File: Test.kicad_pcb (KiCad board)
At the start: 4 copper layers, 171.1 x 129.2 mm, 479 parts, among them P1 CONN_01X02, P18 CONN_01X02, P19 CONN_01X02, P2 CONN_01X02, P24 CONN_01X02, P3 CONN_01X05, P4 CONN_01X04, P8 CONN_01X02, Q1 BSC440N10NS3GATMA1, Q2 BSC440N10NS3GATMA1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

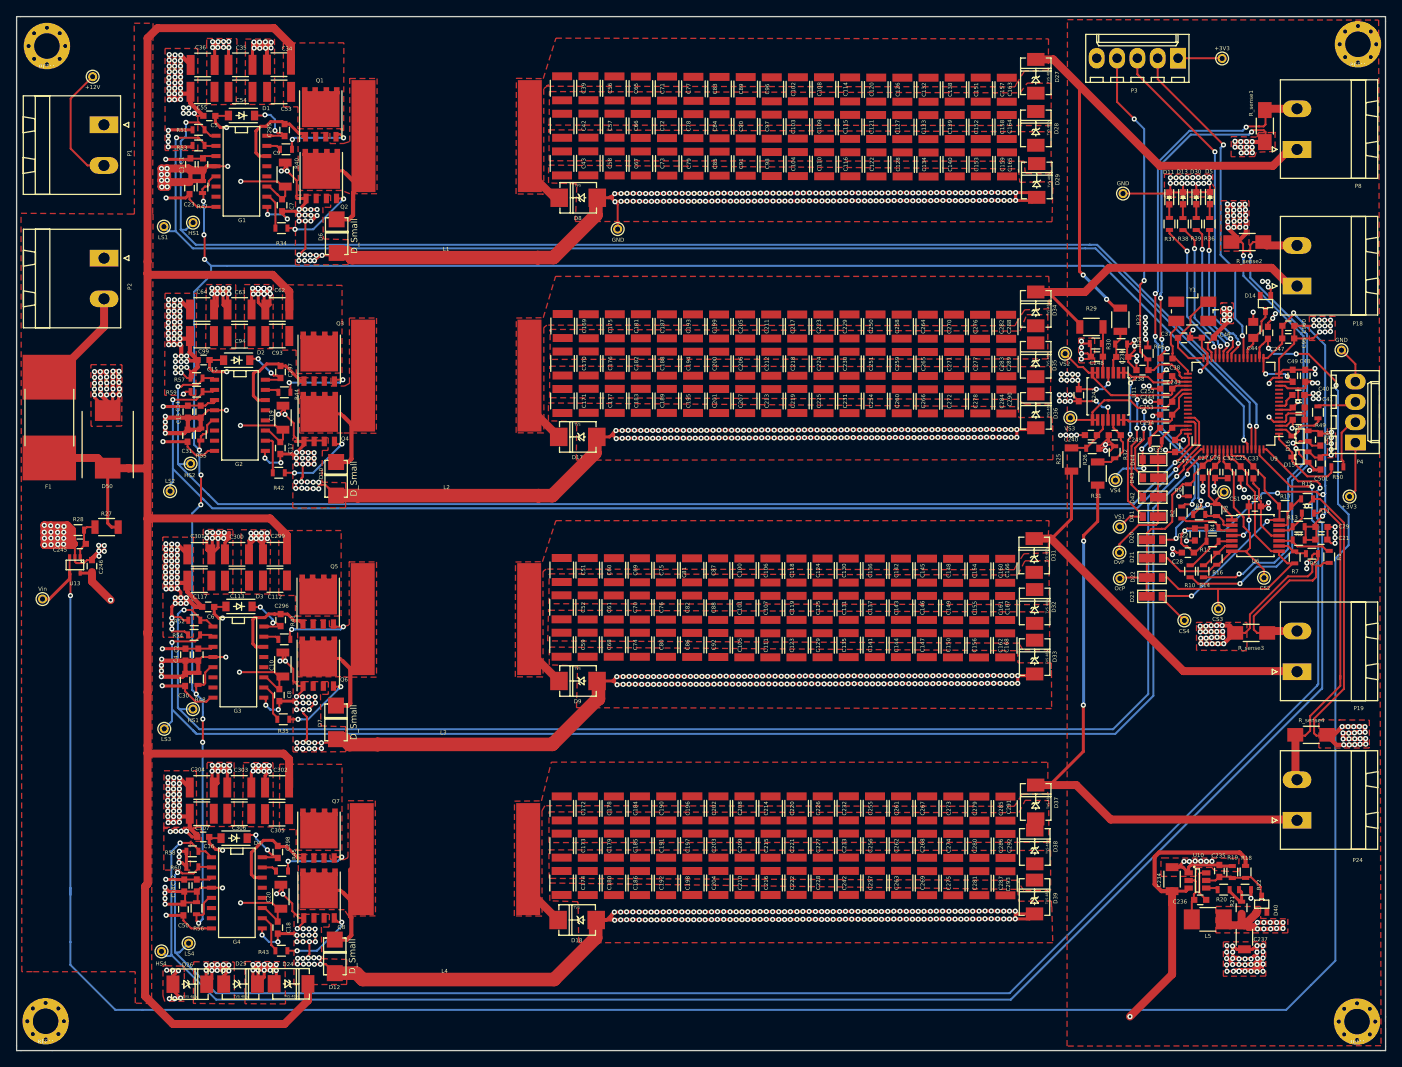
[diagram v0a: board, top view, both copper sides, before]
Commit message: Changed some Diodes footprints to achieve the recommended ones on the datasheet
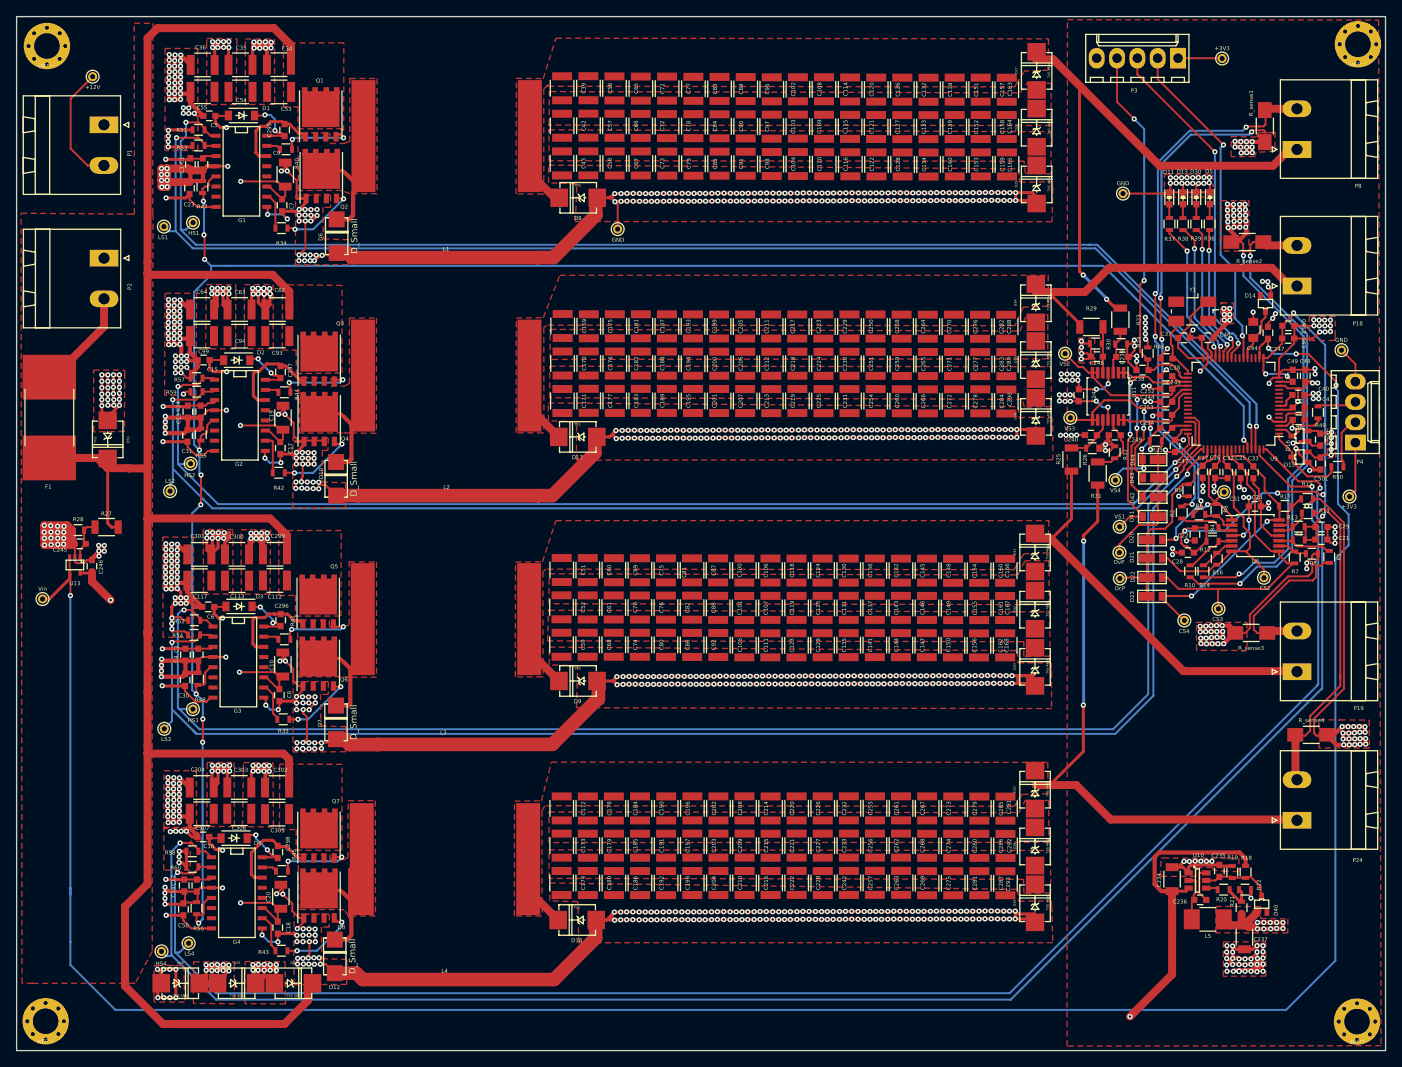
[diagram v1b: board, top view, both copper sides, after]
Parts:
- D24, D25, D26, D27, D28, D29, D31, D32, D33, D34, D35, D36, D37, D38, D39: footprint Eigene Footprints:DO-214AA_TVS_48V -> Eigene Footprints:DO-214AA_TVS_inp
- D50: footprint Diodes_SMD:DO-214AB -> Eigene Footprints:DO-214AA_TVS_inp
- moved D37 1.54 mm to (259.8, 190.2)
- moved D33 1.22 mm to (259.8, 174.8)
- moved D26 1.20 mm to (152.9, 214.3)
- moved D39 0.78 mm to (259.8, 204.3)
- moved D36 0.75 mm to (259.8, 143.6)
- moved D34 0.70 mm to (259.9, 129.3)
- moved D27 0.69 mm to (259.9, 100.3)
- moved D29 0.50 mm to (259.9, 114.5)
- moved D25 0.50 mm to (159.9, 214.3)
- moved D32 0.40 mm to (259.8, 167.7)
- moved D31 0.39 mm to (259.8, 160.5)
- moved D24 0.31 mm to (167.1, 214.3)
- moved D28 0.13 mm to (259.9, 107.4)
- moved D38 0.07 mm to (259.8, 197.2)
- turned D50 to 270 degrees
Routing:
- net GND: track 1547.0 -> 1551.5 mm, vias 1066 -> 1065
- net V_in-: track 253.4 -> 256.2 mm

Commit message: vias under Mosfets more cupper for GND general changes
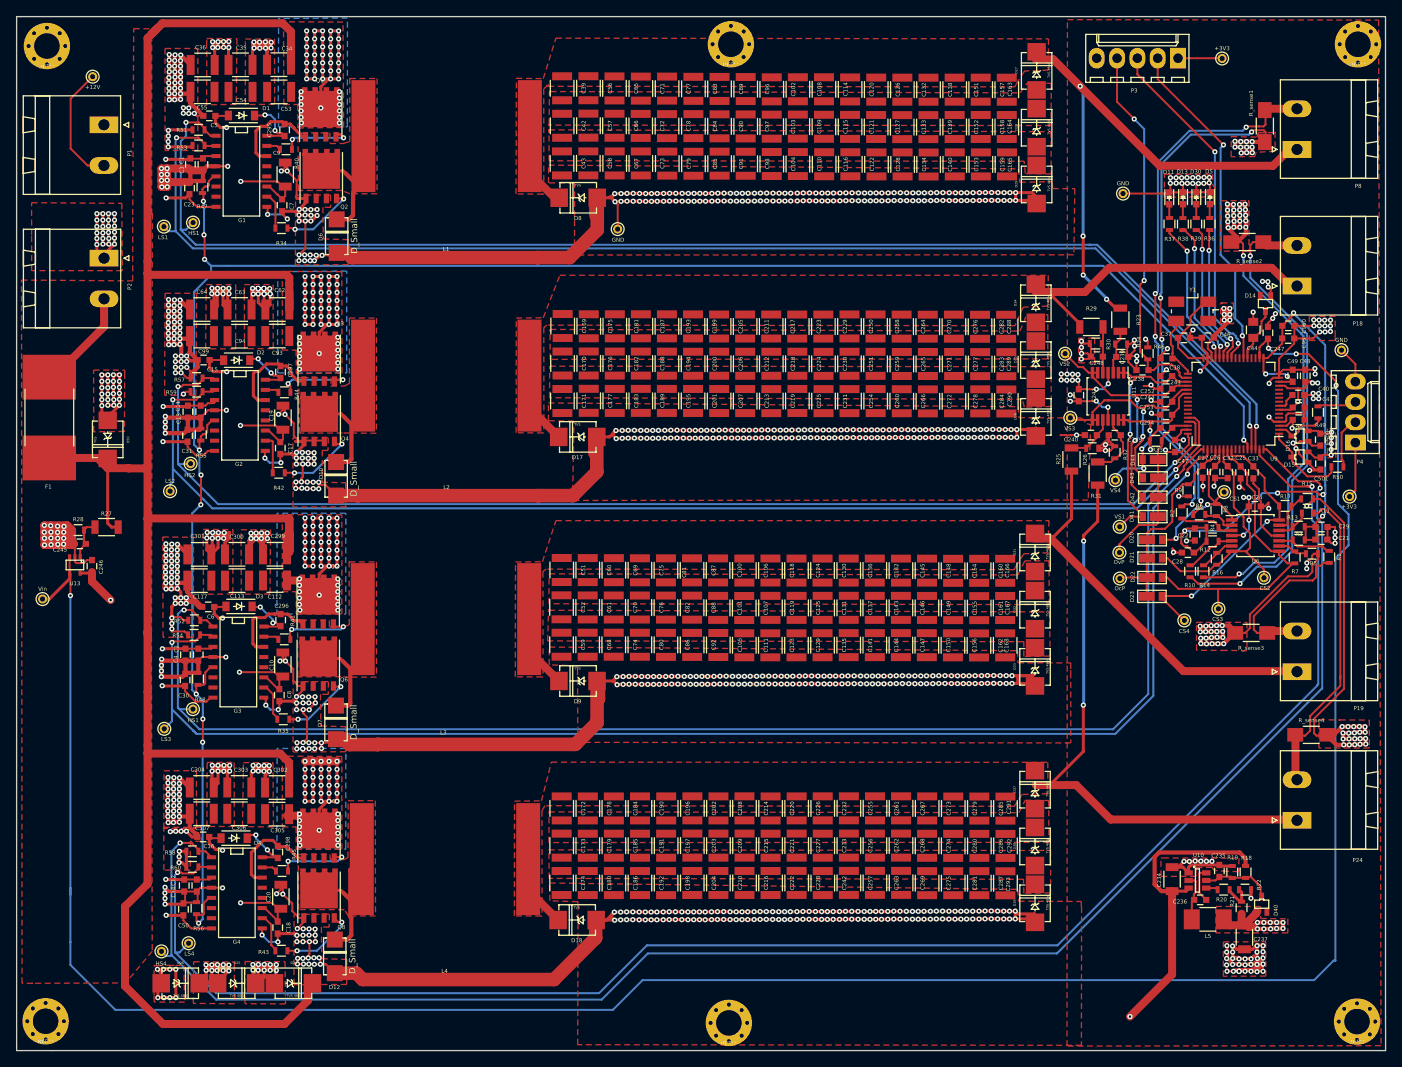
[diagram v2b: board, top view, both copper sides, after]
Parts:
- added REF**: 3mm_holes, Eigene Footprints:3mm_holes, F.Cu at (221.5, 219.3)
- added REF**: 3mm_holes, Eigene Footprints:3mm_holes, F.Cu at (221.7, 97.0)
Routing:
- net V_in-: track 256.2 -> 519.2 mm, vias 0 -> 187
- net GND: track 1551.5 -> 1569.6 mm, vias 1065 -> 1069
- net V_12V: track 388.2 -> 393.1 mm
- net V_out_1: track 84.2 -> 79.4 mm, vias 2 -> 4
- net Sense_Out_Volt_4: track 22.6 -> 24.1 mm
- net +3V3: track 472.9 -> 471.6 mm, vias 57 -> 53
- added copper zone on B.Cu, net V_in-

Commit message: O
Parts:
- G1, G2, G3, G4: footprint SMD_Packages:SO-16-N -> Eigene Footprints:SOIC-16_3.9x9.9mm_Pitch1.27mm
- moved +12V 4.83 mm to (142.2, 96.2)
- moved D4 0.16 mm to (159.7, 196.1)
- moved D2 0.11 mm to (160.0, 136.4)
- moved G1 0.10 mm to (160.4, 112.8), turned to 0 degrees
- moved G3 0.07 mm to (160.2, 174.2), turned to 0 degrees
- moved G2 0.06 mm to (160.4, 143.3), turned to 0 degrees
- turned G4 to 0 degrees
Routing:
- net GND: track 1569.6 -> 1615.2 mm, vias 1069 -> 1091
- net V_12V: track 393.1 -> 384.5 mm
- net (no net): track 2.85 -> 0.00 mm
- net +3V3: track 471.6 -> 469.5 mm, vias 53 -> 48
- net /SW1: track 35.0 -> 37.0 mm
- net /SW4: track 35.2 -> 35.9 mm
- net /SW3: track 22.4 -> 23.1 mm
- net /SW2: track 24.8 -> 25.4 mm
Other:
- board text added: "1"

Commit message: a
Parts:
- moved C9 0.51 mm to (166.0, 113.8)
- moved C7 0.51 mm to (165.6, 117.6)
- moved R40 0.39 mm to (166.1, 110.5)
- moved C17 0.28 mm to (165.3, 147.7)
- moved C19 0.25 mm to (165.7, 143.9)
- moved R44 0.24 mm to (165.9, 140.7)
- moved R34 0.19 mm to (165.5, 120.1)
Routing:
- net V_12V: track 384.5 -> 388.0 mm
- net Net-(G1-Pad15): track 2.14 -> 2.87 mm
- net GND: track 1615.2 -> 1615.8 mm
- net Net-(G2-Pad15): track 2.07 -> 2.59 mm
